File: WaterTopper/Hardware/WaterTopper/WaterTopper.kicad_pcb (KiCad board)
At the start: 2 copper layers, 50 x 80 mm, 37 parts, among them J1 TYPE-C-31-M-12, J2 Barrel_Jack_Switch, J3 Conn_01x07, J4 Conn_01x04, J5 Conn_01x04, J6 Conn_01x04, J7 Conn_01x04, J8 Screw_Terminal_01x02, J9 Screw_Terminal_01x02, U1 AP2112K-3.3, U2 ESP32-S3-MINI-1-N8, U3 DRV8881PRHRT

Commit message: Updated pcb design
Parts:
- added C10: .1u, Capacitor_SMD:C_01005_0402Metric, F.Cu at (196.0, 83.8)
- added C11: .01u, Capacitor_SMD:C_01005_0402Metric, F.Cu at (220.8, 84.5)
- added C12: .01u, Capacitor_SMD:C_01005_0402Metric, F.Cu at (219.2, 81.0)
- added D3: WHITE, LED_SMD:LED_0201_0603Metric, F.Cu at (208.0, 101.5)
- added D4: WHITE, LED_SMD:LED_0201_0603Metric, F.Cu at (206.0, 101.5)
- added D5: WHITE, LED_SMD:LED_0201_0603Metric, F.Cu at (207.0, 101.5)
- added D6: WHITE, LED_SMD:LED_0201_0603Metric, F.Cu at (205.0, 101.5)
- added D7: WHITE, LED_SMD:LED_0201_0603Metric, F.Cu at (204.0, 101.5)
- added D8: WHITE, LED_SMD:LED_0201_0603Metric, F.Cu at (203.0, 101.5)
- added R11: 10k, Resistor_SMD:R_01005_0402Metric, F.Cu at (199.5, 89.8)
- added R12: 20k, Resistor_SMD:R_01005_0402Metric, F.Cu at (196.0, 91.5)
- added R13: 10k, Resistor_SMD:R_01005_0402Metric, F.Cu at (196.8, 91.5)
- added R14: 20k, Resistor_SMD:R_01005_0402Metric, F.Cu at (199.5, 88.5)
- added R15: 2k2, Resistor_SMD:R_01005_0402Metric, F.Cu at (208.0, 103.0)
- added R16: 2k2, Resistor_SMD:R_01005_0402Metric, F.Cu at (206.0, 103.0)
- added R17: 2k2, Resistor_SMD:R_01005_0402Metric, F.Cu at (207.0, 103.0)
- added R18: 2k2, Resistor_SMD:R_01005_0402Metric, F.Cu at (205.0, 103.0)
- added R19: 2k2, Resistor_SMD:R_01005_0402Metric, F.Cu at (204.0, 103.0)
- added R20: 2k2, Resistor_SMD:R_01005_0402Metric, F.Cu at (203.0, 103.0)
- added R21: 10k, Resistor_SMD:R_01005_0402Metric, F.Cu at (200.8, 116.8)
- added SW1: SW_SPST, Button_Switch_SMD:SW_SPST_PTS810, F.Cu at (199.2, 112.0)
- added SW2: SW_SPST, Button_Switch_SMD:SW_SPST_PTS810, F.Cu at (219.5, 112.0)
- added U4: BMP280, Package_LGA:Bosch_LGA-8_2x2.5mm_P0.65mm_ClockwisePinNumbering, F.Cu at (220.0, 82.8)
- C5, C9: value .1u -> .47u
- C7: value .47u -> .1u
- C8: value .1u -> 100u
- J4: footprint Connector_JST:JST_XH_S4B-XH-A-1_1x04_P2.50mm_Horizontal -> Connector_JST:JST_PH_B4B-PH-K_1x04_P2.00mm_Vertical; moved to B.Cu
- J5, J6, J7: footprint Connector_JST:JST_XH_S4B-XH-A_1x04_P2.50mm_Horizontal -> Connector_JST:JST_PH_B4B-PH-K_1x04_P2.00mm_Vertical; moved to B.Cu
- R10: value 20k -> 250m
- R7: value 10k -> 250m
- moved H1 232.9 mm to (96.2, 63.3)
- moved H2 232.9 mm to (140.4, 63.3)
- moved H3 232.9 mm to (96.2, 139.0)
- moved H4 232.9 mm to (140.4, 139.0)
- moved R8 198.6 mm to (207.5, 68.5)
- moved R9 192.0 mm to (193.2, 69.3)
- moved R10 187.1 mm to (193.8, 88.2), turned to 180 degrees
- moved C8 184.4 mm to (192.2, 87.5), turned to -90 degrees
- moved R7 180.4 mm to (193.8, 86.8), turned to 180 degrees
- moved R5 174.8 mm to (207.5, 69.3)
- moved C1 174.3 mm to (220.0, 116.8), turned to -90 degrees
- moved R6 172.3 mm to (193.2, 68.5)
- moved C6 171.7 mm to (193.8, 89.2), turned to 180 degrees
- moved C9 168.5 mm to (193.5, 85.0)
- moved R2 168.4 mm to (192.2, 116.5), turned to 90 degrees
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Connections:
- C5 pad 1: Net-(C5-Pad1) -> /NFAULT
- C5 pad 2: +12V -> GND
- C6 pad 1: Net-(C5-Pad1) -> +12V
- C6 pad 2: +12V -> GND
- C7 pad 1: Net-(C7-Pad1) -> +12V
- C7 pad 2: +12V -> GND
- C8 pad 1: Net-(C8-Pad1) -> +12V
- C8 pad 2: Net-(C8-Pad2) -> GND
- C9 pad 1: GND -> +12V
- C9 pad 2: GND -> Net-(C9-Pad2)
- R7 pad 1: MTR_EN -> Net-(R7-Pad1)
- U2 pad 10: unconnected-(U2-Pad10) -> BMP_SCK
- U2 pad 11: unconnected-(U2-Pad11) -> BMP_SDA
- U2 pad 25: unconnected-(U2-Pad25) -> ULED_1
- U2 pad 26: unconnected-(U2-Pad26) -> ULED_2
- U2 pad 27: unconnected-(U2-Pad27) -> ULED_3
- U2 pad 28: unconnected-(U2-Pad28) -> ULED_4
- U2 pad 29: unconnected-(U2-Pad29) -> ULED_5
- U2 pad 30: unconnected-(U2-Pad30) -> ULED_6
- U2 pad 31: unconnected-(U2-Pad31) -> TFT_SCK
- U2 pad 32: unconnected-(U2-Pad32) -> TFT_SDA
- U2 pad 33: unconnected-(U2-Pad33) -> TFT_RST
- U2 pad 34: unconnected-(U2-Pad34) -> TFT_DC
- U2 pad 35: unconnected-(U2-Pad35) -> TFT_CS
- U2 pad 44: STRAP -> unconnected-(U2-Pad44)
- U2 pad 5: MTR1A -> PWM1
- U2 pad 6: MTR1B -> PWM2
- U2 pad 7: MTR2A -> PWM3
- U2 pad 8: MTR2B -> PWM4
- U3 pad 1: +12V -> Net-(C9-Pad2)
- U3 pad 11: unconnected-(U3-Pad11) -> Net-(R12-Pad1)
- U3 pad 12: unconnected-(U3-Pad12) -> Net-(R12-Pad1)
- U3 pad 13: Net-(C5-Pad1) -> /NFAULT
- U3 pad 16: unconnected-(U3-Pad16) -> Net-(R13-Pad1)
- U3 pad 17: Net-(R10-Pad1) -> Net-(R14-Pad1)
- U3 pad 18: Net-(R10-Pad1) -> Net-(R14-Pad1)
- U3 pad 19: unconnected-(U3-Pad19) -> PWM4
- U3 pad 2: Net-(C7-Pad1) -> +12V
- U3 pad 20: unconnected-(U3-Pad20) -> PWM3
- U3 pad 21: unconnected-(U3-Pad21) -> PWM2
- U3 pad 22: unconnected-(U3-Pad22) -> PWM1
- U3 pad 27: Net-(C8-Pad2) -> Net-(C10-Pad2)
- U3 pad 28: Net-(C8-Pad1) -> Net-(C10-Pad1)
- U3 pad 4: unconnected-(U3-Pad4) -> Net-(R7-Pad1)
- U3 pad 7: unconnected-(U3-Pad7) -> Net-(R10-Pad1)
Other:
- board size 50 x 80 mm -> 192 x 93.5 mm

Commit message: Updated pcb + 4 layer
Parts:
- C1: footprint Capacitor_SMD:C_0201_0603Metric -> Capacitor_SMD:C_0805_2012Metric
- C10, C11, C12, C2, C5, C6, C7, C9: footprint Capacitor_SMD:C_01005_0402Metric -> Capacitor_SMD:C_0603_1608Metric
- C3, C4: footprint Capacitor_SMD:C_01005_0402Metric -> Capacitor_SMD:C_0805_2012Metric
- C8: footprint Capacitor_SMD:C_01005_0402Metric -> Capacitor_SMD:C_Elec_6.3x5.8
- D3, D4, D5, D6, D7, D8: footprint LED_SMD:LED_0201_0603Metric -> LED_SMD:LED_0603_1608Metric
- H1, H2, H3, H4: footprint MountingHole:MountingHole_2.7mm_M2.5 -> MountingHole:MountingHole_3.2mm_M3
- R1, R2, R3, R4, R5, R6, R8, R9: footprint Capacitor_SMD:C_01005_0402Metric -> Resistor_SMD:R_0603_1608Metric
- R10, R11, R12, R13, R14, R15, R16, R17, R18, R19, R20, R21, R7: footprint Resistor_SMD:R_01005_0402Metric -> Resistor_SMD:R_0603_1608Metric
- moved C11 57.0 mm to (163.8, 86.8)
- moved R15 56.4 mm to (166.8, 64.6)
- moved U4 55.7 mm to (164.3, 84.3)
- moved C12 55.5 mm to (163.8, 82.0)
- moved R7 55.4 mm to (138.4, 89.8)
- moved R21 55.3 mm to (145.8, 123.0)
- moved C7 55.1 mm to (138.4, 88.0)
- moved R10 55.1 mm to (138.8, 92.8)
- moved U2 55.1 mm to (154.7, 118.2)
- moved C2 54.8 mm to (163.5, 123.0)
- moved SW2 54.8 mm to (164.8, 113.6)
- moved J5 54.5 mm to (145.0, 64.5)
- moved J8 54.5 mm to (132.5, 82.4)
- moved J9 54.5 mm to (132.5, 93.5)
- moved J7 54.5 mm to (145.0, 72.5)
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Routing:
- net +12V: track 0.00 -> 23.4 mm, vias 0 -> 1
- net Net-(R3-Pad1): track 0.00 -> 18.9 mm, vias 0 -> 2
- net +5V: track 0.00 -> 17.5 mm
- net Net-(R4-Pad1): track 0.00 -> 16.4 mm, vias 0 -> 2
- net GND: track 0.00 -> 13.2 mm, vias 0 -> 14
- net MCU_BOOT: track 0.00 -> 6.89 mm
- net Net-(R13-Pad1): track 0.00 -> 5.58 mm
- net USB_D+: track 0.00 -> 4.69 mm
- net USB_D-: track 0.00 -> 4.29 mm
- net Net-(R14-Pad1): track 0.00 -> 3.86 mm
- net /NFAULT: track 0.00 -> 3.74 mm
- net Net-(R7-Pad1): track 0.00 -> 3.40 mm
- net Net-(C9-Pad2): track 0.00 -> 2.93 mm
- net Net-(R12-Pad1): track 0.00 -> 2.82 mm
- net Net-(D3-Pad2): track 0.00 -> 2.62 mm
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- added copper zone on In2.Cu, net +3V3
- added copper zone on F.Cu, net GND
- added copper zone on In1.Cu, net GND
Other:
- board size 192 x 93.5 mm -> 42.5 x 71 mm
- copper layers 2 -> 4
- rule solder_mask_min_width: 0.12 -> 0.1016

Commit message: Completed pcb v0.1
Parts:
- moved C11 25.9 mm to (150.4, 109.0)
- moved C12 25.9 mm to (150.4, 104.2)
- moved U4 25.6 mm to (151.6, 106.5)
- moved R8 18.5 mm to (134.8, 67.5)
- moved J6 16.8 mm to (145.1, 64.7)
- moved J5 16.3 mm to (159.9, 71.2)
- moved SW1 11.2 mm to (159.8, 106.8), turned to 90 degrees
- moved R6 10.6 mm to (149.5, 69.5)
- moved R19 9.83 mm to (167.8, 115.2)
- moved D1 9.81 mm to (169.8, 115.2)
- moved SW2 6.87 mm to (163.8, 106.8)
- moved R5 4.25 mm to (149.5, 67.5)
- moved R9 4.25 mm to (134.8, 69.5)
- moved D3 4.00 mm to (169.4, 76.6)
- moved D5 4.00 mm to (169.4, 68.6)
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- renumbered D7 to D1, D8 to D2, D4 to D3, D6 to D4, D3 to D5, D5 to D6, D1 to D7, D2 to D8
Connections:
- J9 pad 1: MTR2A -> MTR2B
- J9 pad 2: MTR2B -> MTR2A
- R15 pad 1: ULED_1 -> ULED_5
- R17 pad 1: ULED_2 -> ULED_6
- R19 pad 1: ULED_5 -> ULED_1
- R20 pad 1: ULED_6 -> ULED_2
- U2 pad 10: BMP_SCK -> ULED_5
- U2 pad 11: BMP_SDA -> ULED_6
- U2 pad 12: unconnected-(U2-Pad12) -> TFT_CS
- U2 pad 13: unconnected-(U2-Pad13) -> TFT_DC
- U2 pad 14: unconnected-(U2-Pad14) -> TFT_RST
- U2 pad 15: unconnected-(U2-Pad15) -> TFT_SDA
- U2 pad 16: unconnected-(U2-Pad16) -> TFT_SCK
- U2 pad 17: unconnected-(U2-Pad17) -> LSENSOR1
- U2 pad 18: unconnected-(U2-Pad18) -> LSENSOR2
- U2 pad 19: LSENSOR1 -> LSENSOR3
- U2 pad 20: LSENSOR2 -> LSENSOR4
- U2 pad 21: LSENSOR3 -> BMP_SCK
- U2 pad 22: LSENSOR4 -> BMP_SDA
- U2 pad 25: ULED_1 -> unconnected-(U2-Pad25)
- U2 pad 26: ULED_2 -> unconnected-(U2-Pad26)
- U2 pad 27: ULED_3 -> unconnected-(U2-Pad27)
- U2 pad 28: ULED_4 -> unconnected-(U2-Pad28)
- U2 pad 29: ULED_5 -> unconnected-(U2-Pad29)
- U2 pad 30: ULED_6 -> unconnected-(U2-Pad30)
- U2 pad 31: TFT_SCK -> unconnected-(U2-Pad31)
- U2 pad 32: TFT_SDA -> unconnected-(U2-Pad32)
- U2 pad 33: TFT_RST -> unconnected-(U2-Pad33)
- U2 pad 34: TFT_DC -> PWM1
- U2 pad 35: TFT_CS -> PWM2
- U2 pad 36: unconnected-(U2-Pad36) -> PWM3
- U2 pad 37: unconnected-(U2-Pad37) -> PWM4
- U2 pad 38: unconnected-(U2-Pad38) -> MTR_EN
- U2 pad 5: PWM1 -> ULED_1
- U2 pad 6: PWM2 -> ULED_2
- U2 pad 7: PWM3 -> unconnected-(U2-Pad7)
- U2 pad 8: PWM4 -> ULED_3
- U2 pad 9: MTR_EN -> ULED_4
- U3 pad V1: (no net) -> GND
- U3 pad V2: (no net) -> GND
- U3 pad V3: (no net) -> GND
- U3 pad V4: (no net) -> GND
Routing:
- net +12V: track 23.4 -> 117.4 mm, vias 1 -> 2
- net TFT_SDA: track 0.00 -> 70.4 mm, vias 0 -> 1
- net TFT_CS: track 0.00 -> 68.2 mm, vias 0 -> 1
- net TFT_DC: track 0.00 -> 68.1 mm, vias 0 -> 1
- net TFT_RST: track 0.00 -> 68.1 mm, vias 0 -> 1
- net TFT_SCK: track 0.00 -> 60.2 mm, vias 0 -> 1
- net ULED_6: track 0.00 -> 54.8 mm
- net LSENSOR3: track 0.00 -> 52.9 mm
- net GND: track 13.2 -> 65.8 mm, vias 14 -> 39
- net ULED_5: track 0.00 -> 51.2 mm
- net LSENSOR1: track 0.00 -> 49.3 mm
- net ULED_4: track 0.00 -> 48.8 mm
- net LSENSOR4: track 0.00 -> 46.1 mm
- net ULED_3: track 0.00 -> 43.1 mm
- net LSENSOR2: track 0.00 -> 41.0 mm
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- added copper zone on F.Cu, net (none)
- added copper zone on In1.Cu, net +3V3
- added copper zone on In2.Cu, net GND
- added copper zone on F.Cu, net Net-(C3-Pad1)
- removed copper zone on In2.Cu, net +3V3
- removed copper zone on In1.Cu, net GND

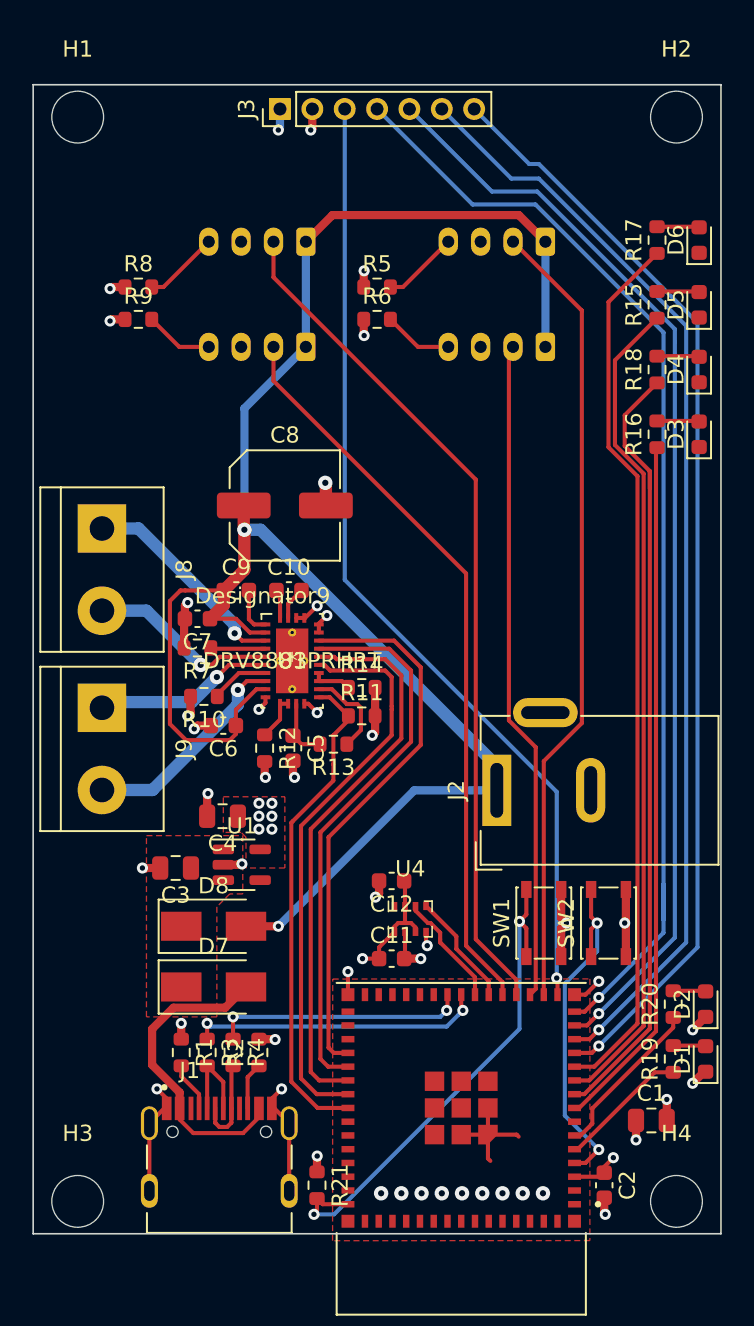
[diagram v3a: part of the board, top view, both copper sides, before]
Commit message: Added/fixed silkscreen
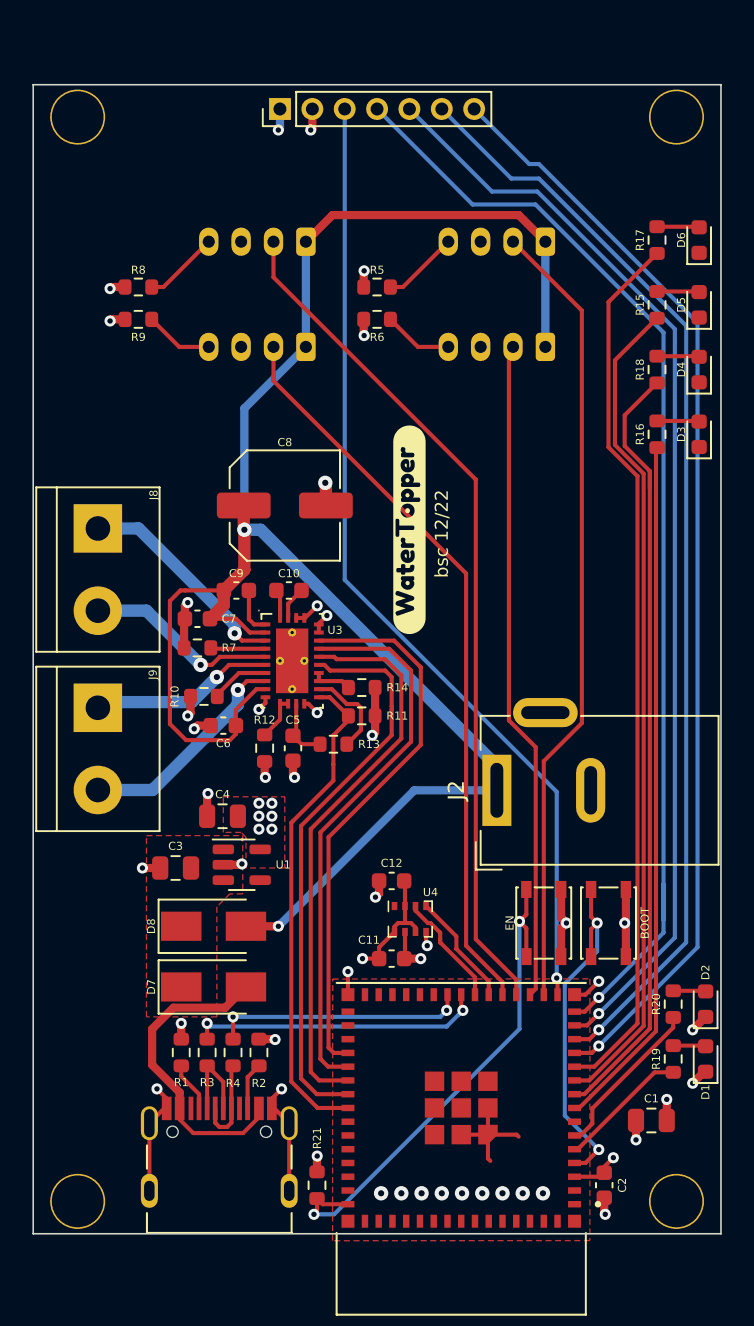
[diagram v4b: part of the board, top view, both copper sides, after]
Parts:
- added kibuzzard-637B1446: G***, kibuzzard-637B1446, F.Cu at (151.5, 82.5)
- moved J8 0.25 mm to (132.2, 82.4)
- moved J9 0.25 mm to (132.2, 93.5)
- renumbered SW2 to BOOT, SW1 to EN
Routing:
- net MTR2B: track 11.2 -> 11.9 mm
- added copper zone on F.Cu, net +3V3
- removed copper zone on F.Cu, net (none)
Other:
- board text added: "bsc 12/22"

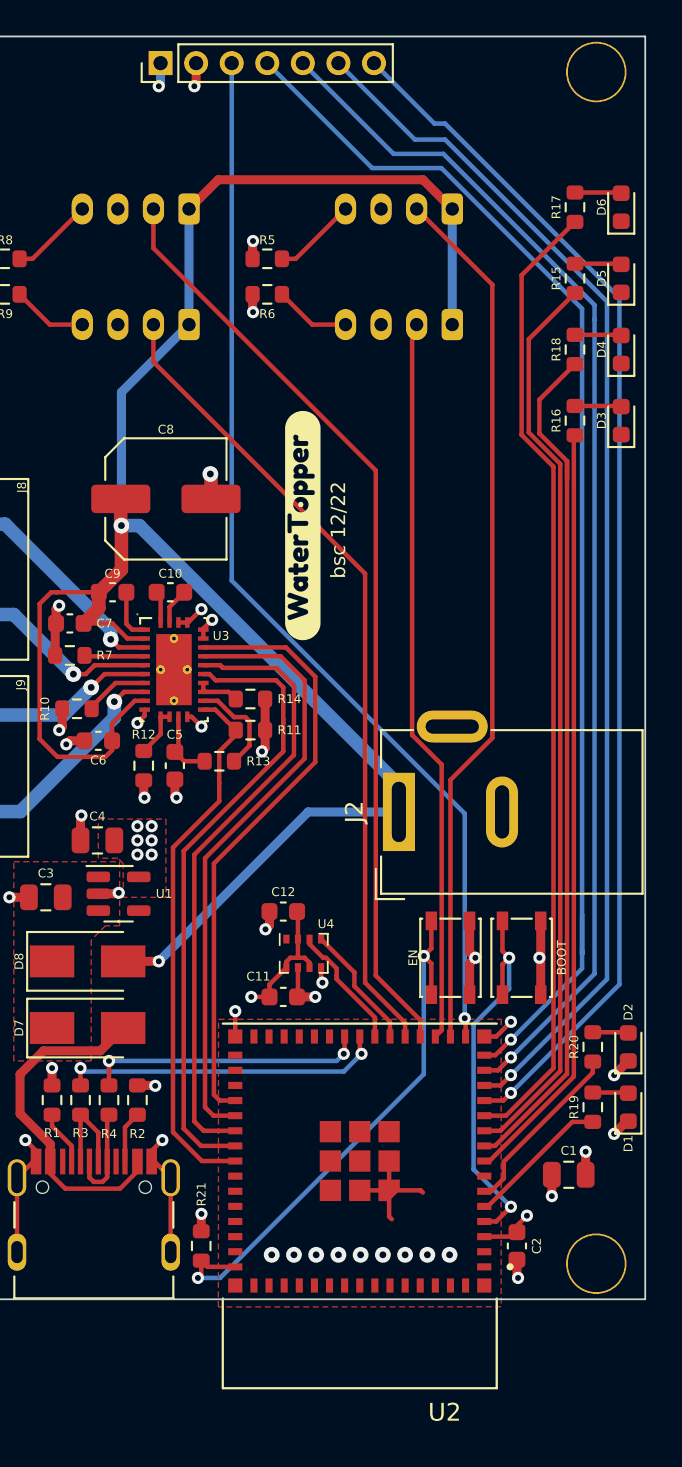
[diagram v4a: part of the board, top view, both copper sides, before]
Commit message: Added small fixes + transistor for display
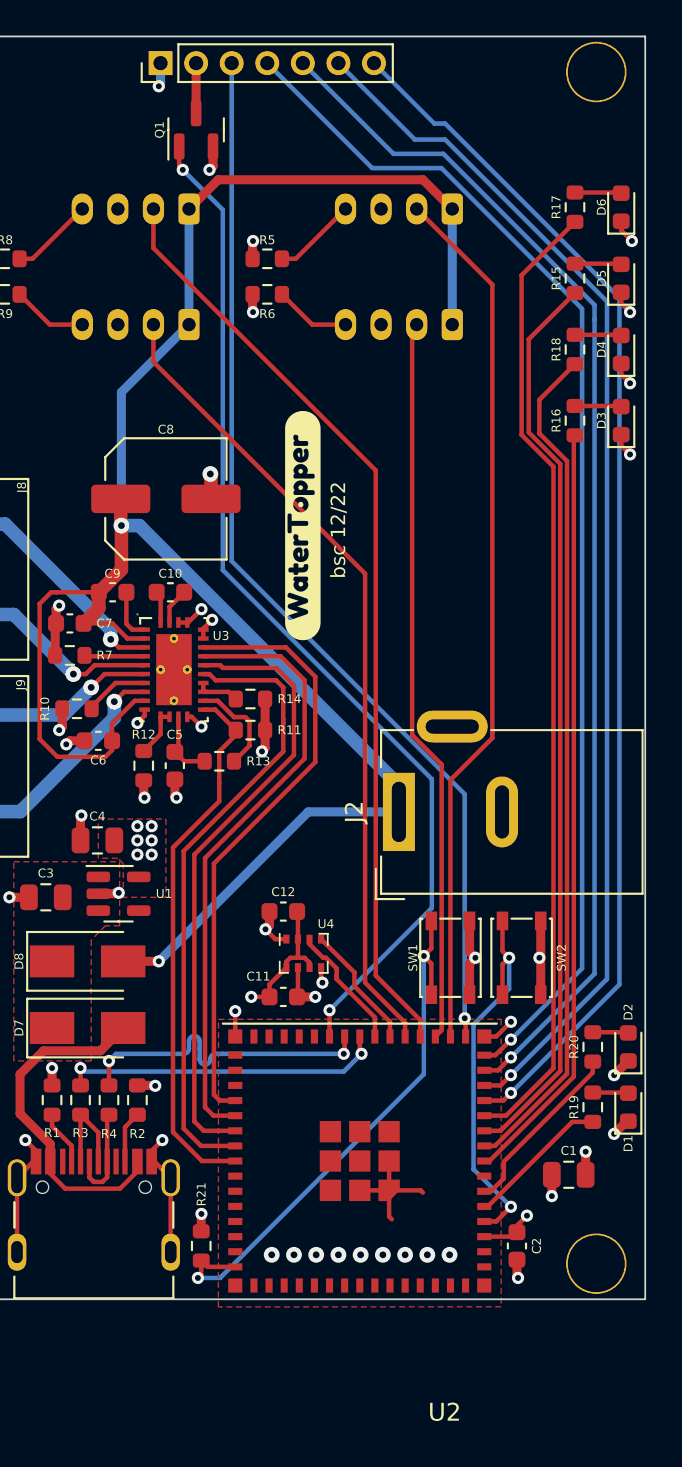
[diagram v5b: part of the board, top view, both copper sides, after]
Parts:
- added Q1: 2N7002, Package_TO_SOT_SMD:SOT-23, F.Cu at (145.5, 60.2)
- renumbered EN to SW1, BOOT to SW2
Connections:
- net Net-(R3-Pad1) renamed /MCU_D-
- net Net-(R4-Pad1) renamed /MCU_D+
- J3 pad 2: +3V3 -> Net-(J3-Pad2)
- U2 pad 25: unconnected-(U2-Pad25) -> TFT_EN
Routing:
- net TFT_EN: track 0.00 -> 58.3 mm, vias 0 -> 2
- net GND: track 65.8 -> 72.6 mm, vias 39 -> 43
- net Net-(J3-Pad2): track 0.00 -> 2.81 mm
- net TFT_SDA: track 70.4 -> 68.0 mm
- net /MCU_D+: track 15.7 -> 18.1 mm
- net +12V: track 117.4 -> 115.5 mm
- net ULED_4: track 48.8 -> 47.7 mm
